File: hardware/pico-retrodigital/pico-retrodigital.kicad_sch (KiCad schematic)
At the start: 23 parts, among them J1 Conn_02x05_Top_Bottom, J2 HDMI_A, J3 Conn_01x04, J6 Conn_01x02_Pin, U1 SN74LVC8T245, U2 SN74LVC8T245, U3 SN74LVC8T245, U4 74LVC2G17, U6 SN74LVC126A, U7 RP2350B

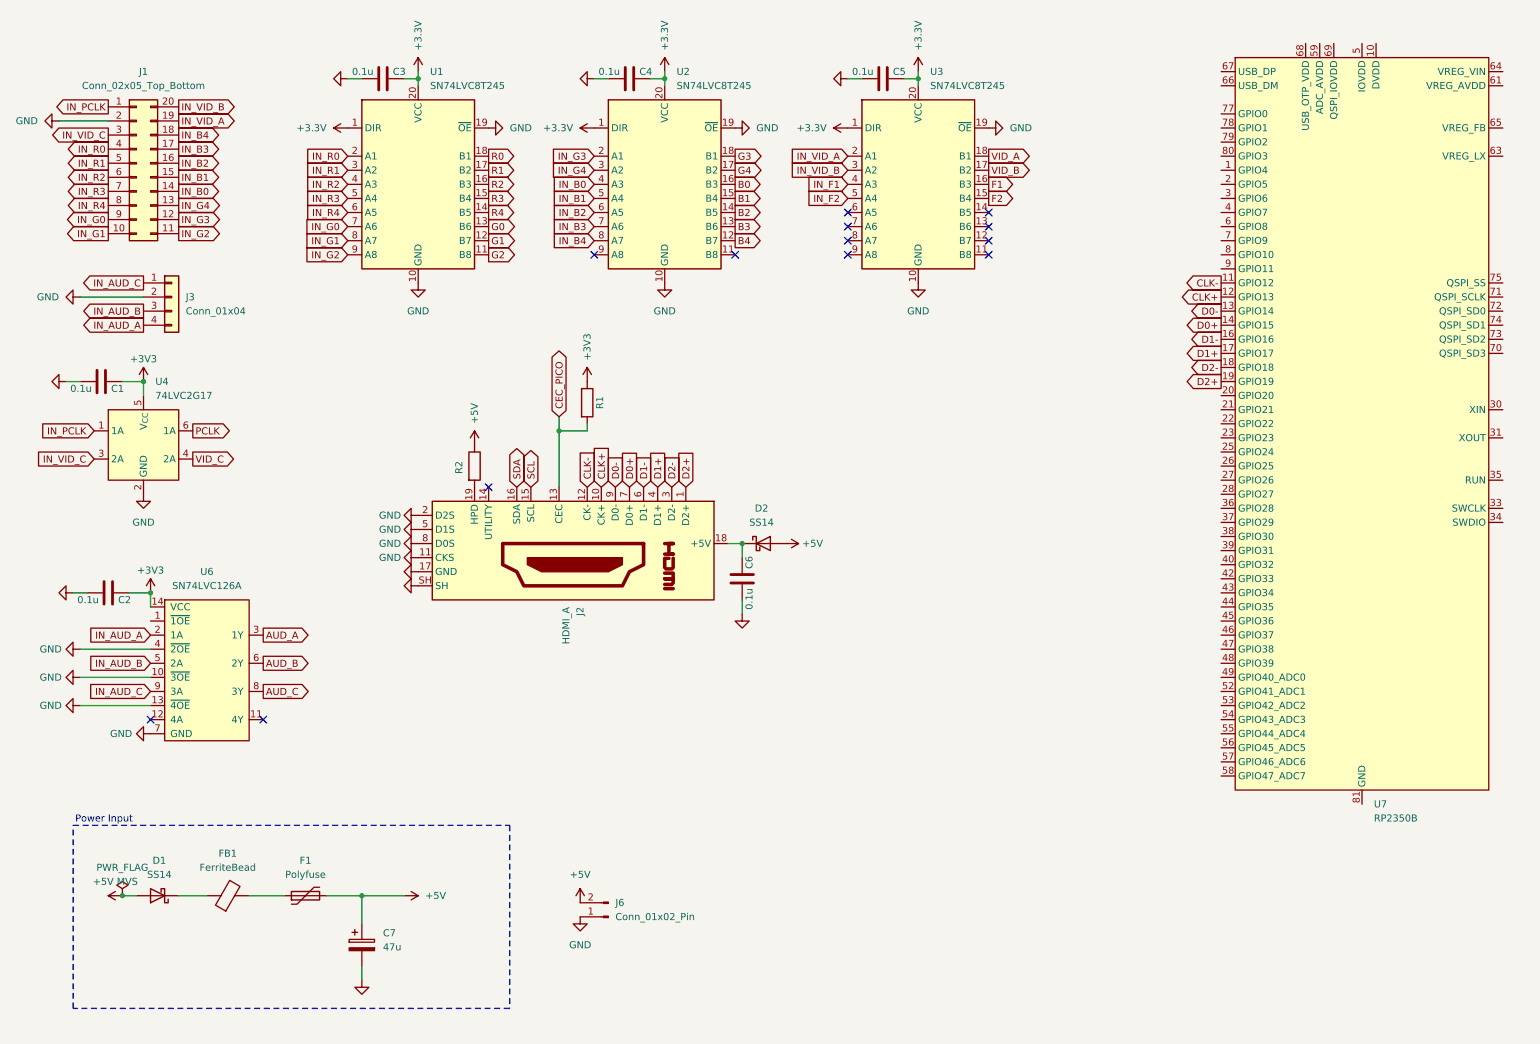
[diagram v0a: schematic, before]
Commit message: Improve audio by adding 2s delay on startup
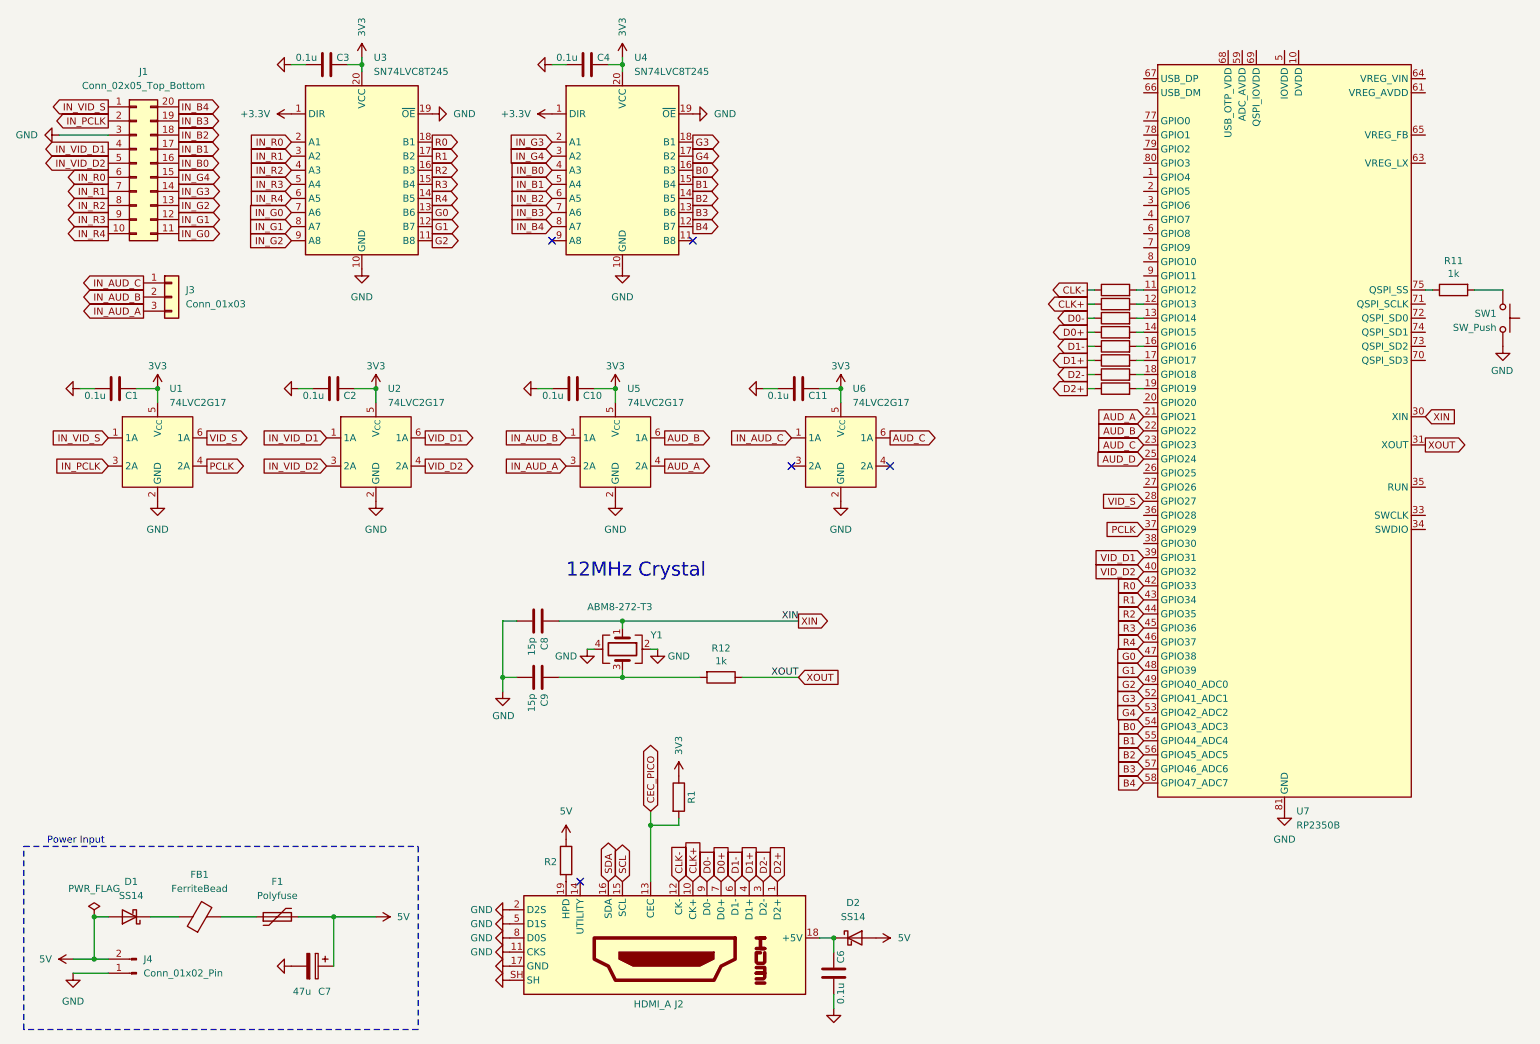
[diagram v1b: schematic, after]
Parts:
- removed C5: 0.1u, Capacitor_SMD:C_0603_1608Metric, symbol Device:C
- removed J6: Conn_01x02_Pin, Connector_PinHeader_2.54mm:PinHeader_1x02_P2.54mm_Vertical, symbol Connector:Conn_01x02_Pin
- removed U3: SN74LVC8T245, custom_components:TSSOP-20_4.4x6.5mm_Pitch0.65mm_Handsoldering, symbol Logic_LevelTranslator:SN74LVC245APW
- removed U6: SN74LVC126A, Package_SO:TSSOP-14_4.4x5mm_P0.65mm, symbol SN74LVC126A:SN74LVC126A
- added C10, C11: 0.1u, Capacitor_SMD:C_0603_1608Metric, symbol Device:C
- added C8, C9: 15p, Capacitor_SMD:C_0402_1005Metric, symbol Device:C
- added J4: Conn_01x02_Pin, Connector_PinHeader_2.54mm:PinHeader_1x02_P2.54mm_Vertical, symbol Connector:Conn_01x02_Pin
- added R10, R3, R4, R5, R6, R7, R8, R9: 220, Resistor_SMD:R_0201_0603Metric, symbol Device:R
- added R11, R12: 1k, Resistor_SMD:R_0402_1005Metric, symbol Device:R
- added SW1: SW_Push, Button_Switch_SMD:SW_Push_1P1T_NO_Vertical_Wuerth_434133025816, symbol Switch:SW_Push
- added U2, U5, U6: 74LVC2G17, Package_TO_SOT_SMD:SOT-23-6, symbol pico-retrodigital:74LVC2G17_SINGLE
- added Y1: ABM8-272-T3, Crystal:Crystal_SMD_3225-4Pin_3.2x2.5mm, symbol Device:Crystal_GND24
- C7: footprint Capacitor_SMD:C_0805_2012Metric -> Capacitor_THT:CP_Radial_D4.0mm_P2.00mm
- J2: Net class (none) -> Power
- J3: value Conn_01x04 -> Conn_01x03; footprint Connector_JST:JST_XA_B04B-XASK-1_1x04_P2.50mm_Vertical -> Connector_PinHeader_2.54mm:PinHeader_1x03_P2.54mm_Vertical; symbol Connector_Generic:Conn_01x04 -> Connector_Generic:Conn_01x03
- renumbered U4 to U1, U1 to U3, U2 to U4
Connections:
- net +5V MVS is gone; now on net 5V: D1.2 (A)
- net IN_VID_A is gone; now on net IN_B3: J1.19 (Pin_19)
- net IN_VID_B is gone; now on net IN_B4: J1.20 (Pin_20)
- net VID_C is gone; now on net PCLK: U1.4 (2A)
- net +3.3V: no longer C3.1, C4.1, U3.20 (VCC), U4.20 (VCC)
- net AUD_A: now also U7.21 (GPIO21), U5.4 (2A)
- net AUD_B: now also U7.22 (GPIO22), U5.6 (1A)
- net AUD_C: now also U7.23 (GPIO23), U6.6 (1A)
- net B0: now also U7.54 (GPIO43_ADC3)
- net B1: now also U7.55 (GPIO44_ADC4)
- net B2: now also U7.56 (GPIO45_ADC5)
- net B3: now also U7.57 (GPIO46_ADC6)
- net B4: now also U7.58 (GPIO47_ADC7)
- net CLK+: now also R5.1; no longer U7.12 (GPIO13)
- net CLK-: now also R4.1; no longer U7.11 (GPIO12)
- net D0+: now also R6.1; no longer U7.14 (GPIO15)
- net D0-: now also R3.1; no longer U7.13 (GPIO14)
- net D1+: now also R8.1; no longer U7.17 (GPIO17)
- net D1-: now also R7.1; no longer U7.16 (GPIO16)
- net D2+: now also R10.1; no longer U7.19 (GPIO19)
- net D2-: now also R9.1; no longer U7.18 (GPIO18)
- net G0: now also U7.47 (GPIO38)
- net G1: now also U7.48 (GPIO39)
- net G2: now also U7.49 (GPIO40_ADC0)
- net G3: now also U7.52 (GPIO41_ADC1)
- net G4: now also U7.53 (GPIO42_ADC2)
- net GND: now also J1.3 (Pin_3), U7.62 (VREG_PGND), U7.81 (GND), C10.2, C11.2, C8.2, C9.2, J4.1 (Pin_1), SW1.1, U2.2 (GND), U5.2 (GND), U6.2 (GND), Y1.2, Y1.4; no longer J1.2 (Pin_2), J3.2 (Pin_2)
- net IN_AUD_A: now also J3.3 (Pin_3), U5.3 (2A); no longer J3.4 (Pin_4)
- net IN_AUD_B: now also J3.2 (Pin_2), U5.1 (1A); no longer J3.3 (Pin_3)
- net IN_AUD_C: now also U6.1 (1A)
- net IN_B0: now also J1.16 (Pin_16); no longer J1.14 (Pin_14)
- net IN_B1: now also J1.17 (Pin_17); no longer J1.15 (Pin_15)
- net IN_B2: now also J1.18 (Pin_18); no longer J1.16 (Pin_16)
- net IN_B3: no longer J1.17 (Pin_17)
- net IN_B4: no longer J1.18 (Pin_18)
- net IN_G0: now also J1.11 (Pin_11); no longer J1.9 (Pin_9)
- net IN_G1: now also J1.12 (Pin_12); no longer J1.10 (Pin_10)
- net IN_G2: now also J1.13 (Pin_13); no longer J1.11 (Pin_11)
- net IN_G3: now also J1.14 (Pin_14); no longer J1.12 (Pin_12)
- net IN_G4: now also J1.15 (Pin_15); no longer J1.13 (Pin_13)
- net IN_PCLK: now also J1.2 (Pin_2), U1.3 (2A); no longer J1.1 (Pin_1), U1.1 (1A)
- net IN_R0: now also J1.6 (Pin_6); no longer J1.4 (Pin_4)
- net IN_R1: now also J1.7 (Pin_7); no longer J1.5 (Pin_5)
- net IN_R2: now also J1.8 (Pin_8); no longer J1.6 (Pin_6)
- net IN_R3: now also J1.9 (Pin_9); no longer J1.7 (Pin_7)
- net IN_R4: now also J1.10 (Pin_10); no longer J1.8 (Pin_8)
- net PCLK: now also U7.37 (GPIO29); no longer U1.6 (1A)
- net R0: now also U7.42 (GPIO33)
- net R1: now also U7.43 (GPIO34)
- net R2: now also U7.44 (GPIO35)
- net R3: now also U7.45 (GPIO36)
- net R4: now also U7.46 (GPIO37)
- net AUD_D: now reaches U7.25 (GPIO24)
- net VID_S: now reaches U7.28 (GPIO27)
- net VID_S: now also U1.6 (1A)
- net XIN: now reaches U7.30 (XIN)
- net XIN: now also C8.1, Y1.1
- net XOUT: now reaches U7.31 (XOUT)
- net XOUT: now also R12.1
- net VID_D1: now reaches U7.39 (GPIO31)
- net VID_D1: now also U2.6 (1A)
- net VID_D2: now reaches U7.40 (GPIO32)
- net VID_D2: now also U2.4 (2A)
- net at U7.75 (QSPI_SS): now also R11.1
- net +3V3 renamed 3V3
- net 3V3: now also C3.1, C4.1, U3.20 (VCC), U4.20 (VCC), C10.1, C11.1, U2.5 (V_{CC}), U5.5 (V_{CC}), U6.5 (V_{CC})
- net +5V renamed 5V
- net 5V: now also J4.2 (Pin_2)
- removed net IN_VID_C: J1.3 (Pin_3), U1.3 (2A)
- new net: C9.1, R12.2, Y1.3
- new net: R11.2, SW1.2
- new net: R6.2, U7.14 (GPIO15)
- new net: R3.2, U7.13 (GPIO14)
- new net: R5.2, U7.12 (GPIO13)
- new net: R9.2, U7.18 (GPIO18)
- new net: R4.2, U7.11 (GPIO12)
- new net: R7.2, U7.16 (GPIO16)
- new net: R10.2, U7.19 (GPIO19)
- new net: R8.2, U7.17 (GPIO17)
- new net IN_VID_D1: J1.4 (Pin_4), U2.1 (1A)
- new net IN_VID_D2: J1.5 (Pin_5), U2.3 (2A)
- new net IN_VID_S: J1.1 (Pin_1), U1.1 (1A)
- no-connect marks 13 -> 5
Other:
- note added: "12MHz Crystal"
- moved on the sheet: C3, C4, C6, C7, D1, D2, F1, FB1, J2, R1, R2, U1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

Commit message: PCB update
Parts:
- added C12, C5: 10u, Capacitor_SMD:C_0805_2012Metric, symbol Device:C
- added J5: USB_C, Connector_USB:USB_Micro-B_Amphenol_10103594-0001LF_Horizontal, symbol Connector:USB_C_Plug_USB2.0
- added R13, R14: 27, Resistor_SMD:R_0402_1005Metric, symbol Device:R
- added U8: NCP1117-3.3_SOT223, Package_TO_SOT_SMD:SOT-223-3_TabPin2, symbol Regulator_Linear:NCP1117-3.3_SOT223
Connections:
- net GND: now also C12.2, C5.2, J5.A1 (GND), J5.A12 (GND), J5.B1 (GND), J5.B12 (GND), J5.S1 (SHIELD), U8.1 (GND)
- net at R11.1: now also SW1.2; no longer U7.75 (QSPI_SS)
- net at R11.2: now also U7.75 (QSPI_SS); no longer SW1.2
- net at U7.66 (USB_DM): now also R14.2
- net at U7.67 (USB_DP): now also R13.2
- new net +3V3: C5.1, U8.2 (VO)
- new net USB_D+: J5.A6 (D+), R13.1
- new net USB_D-: J5.A7 (D-), R14.1
- new net VBUS: C12.1, J5.A4 (VBUS), J5.A9 (VBUS), J5.B4 (VBUS), J5.B9 (VBUS), U8.3 (VI)
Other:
- moved on the sheet: C1, C10, C11, C2, C6, C8, C9, D2, J2, J3, R1, R11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

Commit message: Update PCB
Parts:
- added C13: 4.7u, Capacitor_SMD:C_0402_1005Metric, symbol Device:C
- added C14, C15: 4.7u, RP2350_80QFN_minimal:C_0402_1005Metric_small_pads, symbol Device:C
- added L1: 3.3u, RP2350_80QFN_minimal:L_pol_2016, symbol Device:L
- added R15: 33, Resistor_SMD:R_0402_1005Metric, symbol Device:R
- C12, C5: footprint Capacitor_SMD:C_0805_2012Metric -> Capacitor_SMD:C_0402_1005Metric
- J5: symbol Connector:USB_C_Plug_USB2.0 -> Connector:USB_B_Micro
- renumbered R14 to R13, R13 to R14
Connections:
- net +3V3: now also C1.1, C10.1, C2.1, C3.1, C4.1, R1.1, U1.5 (V_{CC}), U2.5 (V_{CC}), U3.20 (VCC), U4.20 (VCC), U5.5 (V_{CC}), U7.64 (VREG_VIN), C15.1, R15.2
- net 3V3: no longer C1.1, C10.1, C2.1, C3.1, C4.1, R1.1, U1.5 (V_{CC}), U2.5 (V_{CC}), U3.20 (VCC), U4.20 (VCC), U5.5 (V_{CC})
- net GND: now also J5.5 (GND), J5.6 (Shield), C13.2, C14.1, C15.2; no longer J5.A1 (GND), J5.A12 (GND), J5.B1 (GND), J5.B12 (GND), J5.S1 (SHIELD)
- net USB_D+: now also J5.3 (D+); no longer J5.A6 (D+)
- net USB_D-: now also J5.2 (D-); no longer J5.A7 (D-)
- net VBUS: now also J5.1 (VBUS); no longer J5.A4 (VBUS), J5.A9 (VBUS), J5.B4 (VBUS), J5.B9 (VBUS)
- net at U7.61 (VREG_AVDD): now also C13.1, R15.1
- net at U7.63 (VREG_LX): now also L1.2
- net +1V1: now reaches U7.65 (VREG_FB)
- net +1V1: now also C14.2, L1.1
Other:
- moved on the sheet: C11, C12, C5, C6, D2, J2, R1, R11, R13, R14, R2, SW1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

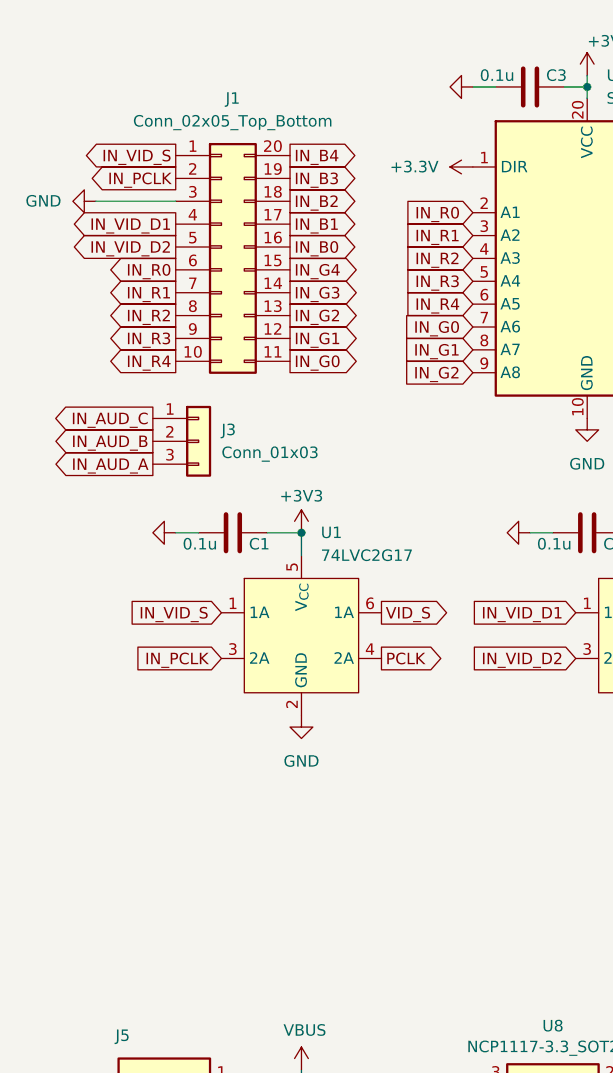
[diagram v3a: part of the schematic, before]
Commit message: Git ignore
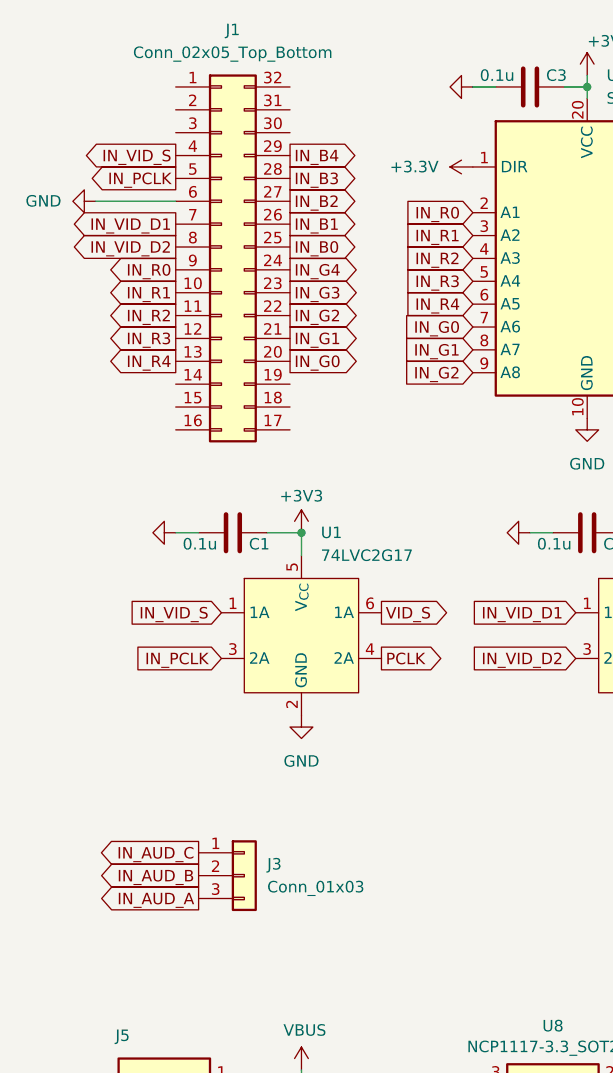
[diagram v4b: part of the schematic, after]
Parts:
- J1: symbol Connector_Generic:Conn_02x10_Counter_Clockwise -> Connector_Generic:Conn_02x16_Counter_Clockwise
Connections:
- net GND: now also J1.6 (Pin_6); no longer J1.3 (Pin_3)
- net IN_B0: now also J1.25 (Pin_25); no longer J1.16 (Pin_16)
- net IN_B1: now also J1.26 (Pin_26); no longer J1.17 (Pin_17)
- net IN_B2: now also J1.27 (Pin_27); no longer J1.18 (Pin_18)
- net IN_B3: now also J1.28 (Pin_28); no longer J1.19 (Pin_19)
- net IN_B4: now also J1.29 (Pin_29); no longer J1.20 (Pin_20)
- net IN_G0: now also J1.20 (Pin_20); no longer J1.11 (Pin_11)
- net IN_G1: now also J1.21 (Pin_21); no longer J1.12 (Pin_12)
- net IN_G2: now also J1.22 (Pin_22); no longer J1.13 (Pin_13)
- net IN_G3: now also J1.23 (Pin_23); no longer J1.14 (Pin_14)
- net IN_G4: now also J1.24 (Pin_24); no longer J1.15 (Pin_15)
- net IN_PCLK: now also J1.5 (Pin_5); no longer J1.2 (Pin_2)
- net IN_R0: now also J1.9 (Pin_9); no longer J1.6 (Pin_6)
- net IN_R1: now also J1.10 (Pin_10); no longer J1.7 (Pin_7)
- net IN_R2: now also J1.11 (Pin_11); no longer J1.8 (Pin_8)
- net IN_R3: now also J1.12 (Pin_12); no longer J1.9 (Pin_9)
- net IN_R4: now also J1.13 (Pin_13); no longer J1.10 (Pin_10)
- net IN_VID_D1: now also J1.7 (Pin_7); no longer J1.4 (Pin_4)
- net IN_VID_D2: now also J1.8 (Pin_8); no longer J1.5 (Pin_5)
- net IN_VID_S: now also J1.4 (Pin_4); no longer J1.1 (Pin_1)
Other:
- moved on the sheet: J3
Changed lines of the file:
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@@
 	(global_label "IN_AUD_B"
 		(shape output)
-		(at 26.67 60.96 180)
+		(at 31.75 109.22 180)
 		(fields_autoplaced yes)
 		(effects
@@
 		)
 		(property "Intersheetrefs" "${INTERSHEET_REFS}"
-			(at 14.8552 60.96 0)
+			(at 19.9352 109.22 0)
 			(effects
 				(font
@@
 	(global_label "IN_AUD_C"
 		(shape output)
-		(at 26.67 58.42 180)
+		(at 31.75 106.68 180)
 		(fields_autoplaced yes)
 		(effects
@@
 		)
 		(property "Intersheetrefs" "${INTERSHEET_REFS}"
-			(at 14.8552 58.42 0)
+			(at 19.9352 106.68 0)
 			(effects
 				(font
@@
 	(global_label "IN_AUD_A"
 		(shape output)
-		(at 26.67 63.5 180)
+		(at 31.75 111.76 180)
 		(fields_autoplaced yes)
 		(effects
@@
 		)
 		(property "Intersheetrefs" "${INTERSHEET_REFS}"
-			(at 15.0366 63.5 0)
+			(at 20.1166 111.76 0)
 			(effects
 				(font
@@
 	)
 	(symbol
-		(lib_id "Connector_Generic:Conn_02x10_Counter_Clockwise")
+		(lib_id "Connector_Generic:Conn_02x16_Counter_Clockwise")
 		(at 34.29 39.37 0)
 		(unit 1)
@@
 		(fields_autoplaced yes)
 		(property "Reference" "J1"
-			(at 35.56 22.86 0)
+			(at 35.56 15.24 0)
 			(effects
 				(font
@@
 		)
 		(property "Value" "Conn_02x05_Top_Bottom"
-			(at 35.56 25.4 0)
+			(at 35.56 17.78 0)
 			(effects
 				(font
@@
 			)
 		)
-		(property "Description" "Generic connector, double row, 02x10, counter clockwise pin numbering scheme (similar to DIP package numbering), script generated (kicad-library-utils/schlib/autogen/connector/)"
+		(property "Description" "Generic connector, double row, 02x16, counter clockwise pin numbering scheme (similar to DIP package numbering), script generated (kicad-library-utils/schlib/autogen/connector/)"
 			(at 34.29 39.37 0)
 			(effects
@@
 		(pin "11"
 		)
+		(pin "23"
+		)
+		(pin "27"
+		)
+		(pin "24"
+		)
+		(pin "25"
+		)
+		(pin "28"
+		)
+		(pin "22"
+		)
+		(pin "26"
+		)
+		(pin "21"
+		)
+		(pin "30"
+		)
+		(pin "29"
+		)
+		(pin "32"
+		)
+		(pin "31"
+		)
 		(instances
 			(project "pico-retrodigital"
@@
 	(symbol
 		(lib_id "Connector_Generic:Conn_01x03")
-		(at 31.75 60.96 0)
+		(at 36.83 109.22 0)
 		(unit 1)
 		(exclude_from_sim no)
@@
 		(dnp no)
 		(property "Reference" "J3"
-			(at 34.29 59.6899 0)
+			(at 39.37 107.9499 0)
 			(effects
 				(font
@@
 		)
 		(property "Value" "Conn_01x03"
-			(at 34.29 62.2299 0)
+			(at 39.37 110.4899 0)
 			(effects
 				(font
@@
 		)
 		(property "Footprint" "Connector_PinHeader_2.54mm:PinHeader_1x03_P2.54mm_Vertical"
-			(at 27.686 71.628 0)
+			(at 32.766 119.888 0)
 			(effects
 				(font
@@
 		)
 		(property "Datasheet" "~"
-			(at 31.75 60.96 0)
+			(at 36.83 109.22 0)
 			(effects
 				(font
@@
 		)
 		(property "Description" "Generic connector, single row, 01x03, script generated (kicad-library-utils/schlib/autogen/connector/)"
-			(at 31.75 60.96 0)
+			(at 36.83 109.22 0)
 			(effects
 				(font
